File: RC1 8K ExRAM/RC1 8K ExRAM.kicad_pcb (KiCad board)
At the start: 2 copper layers, 99.1 x 83.8 mm, 29 parts, among them J1 Expansion, J2 ADDRESS, U1 74LS138, U2 74LS00, U3 74HC595, U4 74HC595, U5 HM62256BLP-7, U6 74LS244, U7 74LS244, U8 74LS245

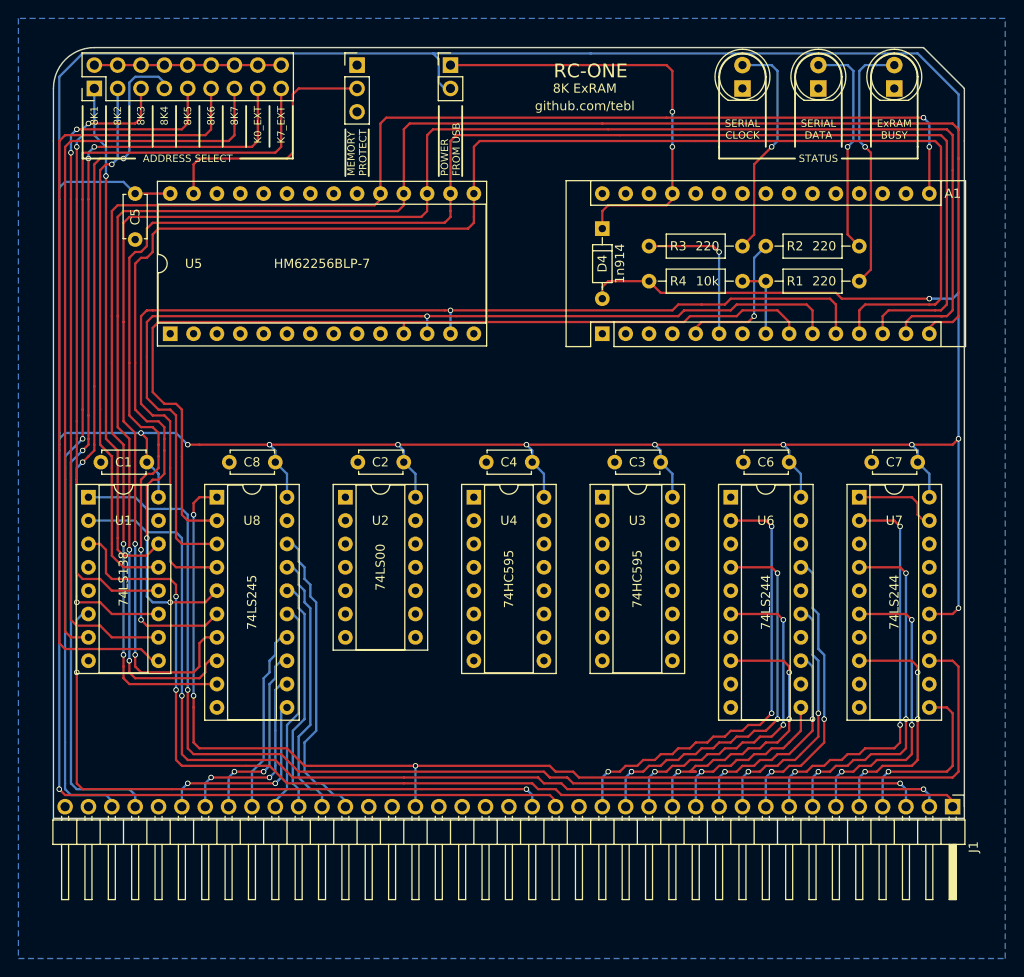
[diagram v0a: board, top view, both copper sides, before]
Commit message: 8K ExRAM layout and silkscreen done
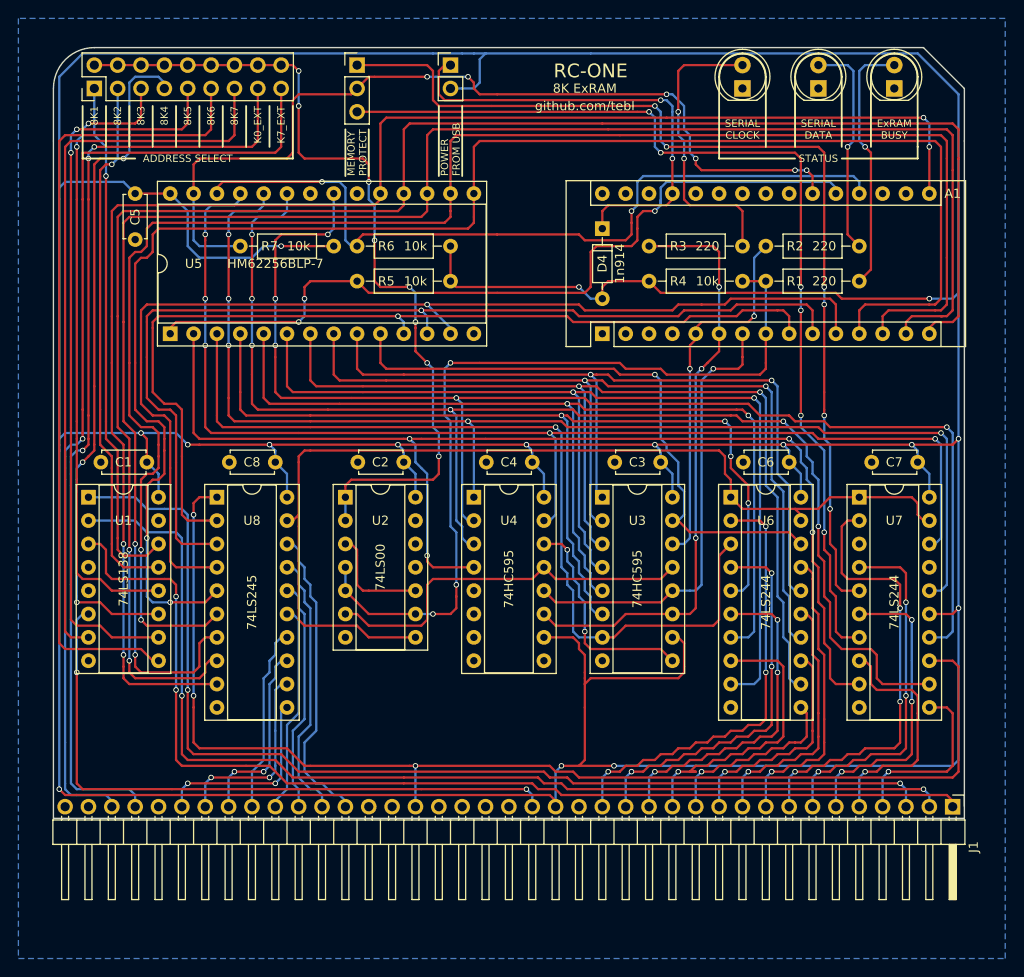
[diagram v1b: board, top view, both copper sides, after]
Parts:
- added R5: 10k, Resistors_THT:R_Axial_DIN0207_L6.3mm_D2.5mm_P10.16mm_Horizontal, F.Cu at (128.3, 90.2)
- added R6: 10k, Resistors_THT:R_Axial_DIN0207_L6.3mm_D2.5mm_P10.16mm_Horizontal, F.Cu at (128.3, 86.4)
- added R7: 10k, Resistors_THT:R_Axial_DIN0207_L6.3mm_D2.5mm_P10.16mm_Horizontal, F.Cu at (115.6, 86.4)
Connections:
- A1 pad 19: (no net) -> /EX_A13
- A1 pad 20: (no net) -> /EX_A14
- A1 pad 21: (no net) -> /EX_R/~W
- U4 pad 7: /EX_R/~W -> (no net)
- U5 pad 1: GND -> /EX_A14
- U5 pad 26: GND -> /EX_A13
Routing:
- net VCC: track 497.4 -> 643.1 mm, vias 12 -> 16
- net /EX_A10: track 0.00 -> 141.6 mm, vias 0 -> 5
- net /EX_A11: track 0.00 -> 140.5 mm, vias 0 -> 6
- net /EX_A9: track 0.00 -> 132.9 mm, vias 0 -> 5
- net /EX_A8: track 0.00 -> 131.6 mm, vias 0 -> 5
- net /EX_A12: track 0.00 -> 126.6 mm, vias 0 -> 4
- net /EX_A4: track 0.00 -> 112.6 mm, vias 0 -> 2
- net /EX_A5: track 0.00 -> 109.9 mm, vias 0 -> 2
- net Net-(JP2-Pad1): track 0.00 -> 108.8 mm, vias 0 -> 6
- net Net-(JP2-Pad3): track 0.00 -> 108.0 mm, vias 0 -> 6
- net /EX_A3: track 0.00 -> 107.0 mm, vias 0 -> 2
- net /EX_A6: track 0.00 -> 106.9 mm, vias 0 -> 4
- net ~EXT_CS: track 9.42 -> 110.4 mm
- net /EX_A2: track 0.00 -> 97.6 mm, vias 0 -> 2
- net /EX_A7: track 0.00 -> 95.3 mm, vias 0 -> 1
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
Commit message: Gerber export
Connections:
- A1 pad 26: (no net) -> /RESET
- J1 pad 20: (no net) -> /RESET
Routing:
- net /RESET: track 0.00 -> 101.1 mm, vias 0 -> 6
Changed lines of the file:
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@@
 (kicad_pcb (version 4) (host pcbnew 4.0.7)
   (general
-    (links 176)
+    (links 177)
     (no_connects 0)
-    (area 91.44 61.595 198.755001 163.830001)
+    (area 95.174999 64.694999 194.385001 148.665001)
     (thickness 1.6)
     (drawings 140)
-    (tracks 1760)
+    (tracks 1793)
     (zones 0)
     (modules 32)
-    (nets 77)
+    (nets 78)
   )
   (page A4)
@@
   (net 75 /EX_A13)
   (net 76 /EX_A14)
+  (net 77 /RESET)
   (net_class Default "This is the default net class."
     (clearance 0.2)
@@
     (add_net /PHI2)
     (add_net /R/~W)
+    (add_net /RESET)
     (add_net BUS_EN)
     (add_net GND)
@@
     (pad 10 thru_hole oval (at 0 22.86 90) (size 1.6 1.6) (drill 0.8) (layers *.Cu *.Mask)
       (net 7 /EX_D1))
-    (pad 26 thru_hole oval (at 15.24 10.16 90) (size 1.6 1.6) (drill 0.8) (layers *.Cu *.Mask))
+    (pad 26 thru_hole oval (at 15.24 10.16 90) (size 1.6 1.6) (drill 0.8) (layers *.Cu *.Mask)
+      (net 77 /RESET))
     (pad 11 thru_hole oval (at 0 25.4 90) (size 1.6 1.6) (drill 0.8) (layers *.Cu *.Mask)
       (net 8 /EX_D2))
@@
     (pad 19 thru_hole oval (at 0 45.72 270) (size 1.7 1.7) (drill 1) (layers *.Cu *.Mask)
       (net 32 /PHI2))
-    (pad 20 thru_hole oval (at 0 48.26 270) (size 1.7 1.7) (drill 1) (layers *.Cu *.Mask))
+    (pad 20 thru_hole oval (at 0 48.26 270) (size 1.7 1.7) (drill 1) (layers *.Cu *.Mask)
+      (net 77 /RESET))
     (pad 21 thru_hole oval (at 0 50.8 270) (size 1.7 1.7) (drill 1) (layers *.Cu *.Mask))
     (pad 22 thru_hole oval (at 0 53.34 270) (size 1.7 1.7) (drill 1) (layers *.Cu *.Mask))
@@
   (segment (start 139.065 123.19) (end 139.065 124.46) (width 0.25) (layer F.Cu) (net 5))
   (segment (start 138.43 116.84) (end 139.065 117.475) (width 0.25) (layer B.Cu) (net 5))
-  (segment (start 136.525 126.365) (end 134.62 126.365) (width 0.25) (layer B.Cu) (net 5))
-  (via (at 136.525 126.365) (size 0.6) (drill 0.4) (layers F.Cu B.Cu) (net 5))
-  (segment (start 138.43 126.365) (end 136.525 126.365) (width 0.25) (layer F.Cu) (net 5))
+  (segment (start 137.16 126.365) (end 134.62 126.365) (width 0.25) (layer B.Cu) (net 5))
+  (via (at 137.16 126.365) (size 0.6) (drill 0.4) (layers F.Cu B.Cu) (net 5))
+  (segment (start 138.43 126.365) (end 137.16 126.365) (width 0.25) (layer F.Cu) (net 5))
   (segment (start 139.065 125.73) (end 138.43 126.365) (width 0.25) (layer F.Cu) (net 5))
   (segment (start 137.795 104.775) (end 137.795 102.87) (width 0.25) (layer B.Cu) (net 5))
@@
   (segment (start 107.95 95.25) (end 108.585 94.615) (width 0.25) (layer F.Cu) (net 76))
   (segment (start 107.95 95.885) (end 107.95 95.25) (width 0.25) (layer F.Cu) (net 76))
+  (segment (start 151.765 90.17) (end 151.765 85.725) (width 0.25) (layer F.Cu) (net 77))
+  (segment (start 152.4 83.185) (end 153.035 83.185) (width 0.25) (layer B.Cu) (net 77))
+  (segment (start 151.765 83.82) (end 152.4 83.185) (width 0.25) (layer B.Cu) (net 77))
+  (segment (start 151.765 85.725) (end 151.765 83.82) (width 0.25) (layer B.Cu) (net 77))
+  (via (at 151.765 85.725) (size 0.6) (drill 0.4) (layers F.Cu B.Cu) (net 77))
+  (segment (start 151.765 95.25) (end 151.765 97.79) (width 0.25) (layer F.Cu) (net 77))
+  (via (at 136.525 123.825) (size 0.6) (drill 0.4) (layers F.Cu B.Cu) (net 77))
+  (segment (start 136.525 123.825) (end 136.525 118.11) (width 0.25) (layer B.Cu) (net 77))
+  (segment (start 136.525 118.11) (end 137.795 116.84) (width 0.25) (layer B.Cu) (net 77))
+  (segment (start 137.795 116.84) (end 137.795 106.045) (width 0.25) (layer B.Cu) (net 77))
+  (segment (start 137.795 106.045) (end 137.16 105.41) (width 0.25) (layer B.Cu) (net 77))
+  (segment (start 137.16 105.41) (end 137.16 99.06) (width 0.25) (layer B.Cu) (net 77))
+  (via (at 137.16 99.06) (size 0.6) (drill 0.4) (layers F.Cu B.Cu) (net 77))
+  (via (at 144.145 142.24) (size 0.6) (drill 0.4) (layers F.Cu B.Cu) (net 77))
+  (segment (start 144.145 142.24) (end 139.065 142.24) (width 0.25) (layer F.Cu) (net 77))
+  (segment (start 144.78 147.32) (end 144.78 142.875) (width 0.25) (layer B.Cu) (net 77))
+  (segment (start 144.78 142.875) (end 144.145 142.24) (width 0.25) (layer B.Cu) (net 77))
+  (segment (start 136.525 127.635) (end 136.525 123.825) (width 0.25) (layer F.Cu) (net 77))
+  (segment (start 136.525 141.605) (end 137.16 142.24) (width 0.25) (layer F.Cu) (net 77))
+  (segment (start 137.16 142.24) (end 139.065 142.24) (width 0.25) (layer F.Cu) (net 77))
+  (segment (start 136.525 127.635) (end 136.525 141.605) (width 0.25) (layer F.Cu) (net 77))
+  (via (at 151.765 90.17) (size 0.6) (drill 0.4) (layers F.Cu B.Cu) (net 77))
+  (segment (start 151.765 90.17) (end 151.765 95.25) (width 0.25) (layer B.Cu) (net 77))
+  (via (at 151.765 95.25) (size 0.6) (drill 0.4) (layers F.Cu B.Cu) (net 77))
+  (segment (start 165.1 81.915) (end 165.1 80.645) (width 0.25) (layer B.Cu) (net 77))
+  (segment (start 153.67 83.185) (end 153.035 83.185) (width 0.25) (layer B.Cu) (net 77))
+  (segment (start 161.29 83.185) (end 153.67 83.185) (width 0.25) (layer B.Cu) (net 77))
+  (segment (start 161.925 82.55) (end 161.29 83.185) (width 0.25) (layer B.Cu) (net 77))
+  (segment (start 164.465 82.55) (end 161.925 82.55) (width 0.25) (layer B.Cu) (net 77))
+  (segment (start 165.1 81.915) (end 164.465 82.55) (width 0.25) (layer B.Cu) (net 77))
+  (segment (start 137.795 98.425) (end 137.16 99.06) (width 0.25) (layer F.Cu) (net 77))
+  (segment (start 151.13 98.425) (end 137.795 98.425) (width 0.25) (layer F.Cu) (net 77))
+  (segment (start 151.765 97.79) (end 151.13 98.425) (width 0.25) (layer F.Cu) (net 77))
   (zone (net 1) (net_name GND) (layer B.Cu) (hatch edge 0.508)
     (connect_pads (clearance 0.508))

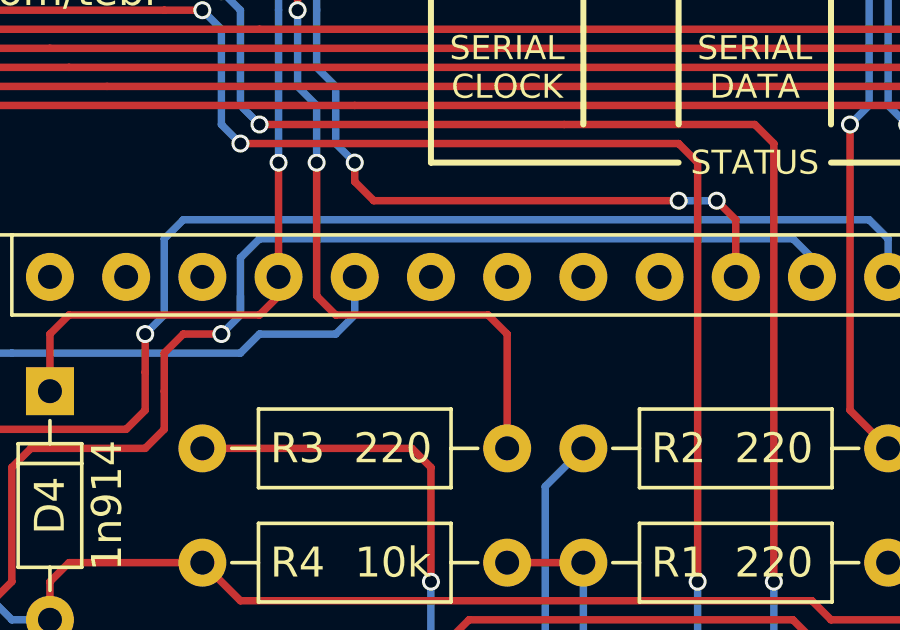
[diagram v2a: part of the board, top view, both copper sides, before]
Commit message: A7 not usable as digital pin on Nano (appearantly)
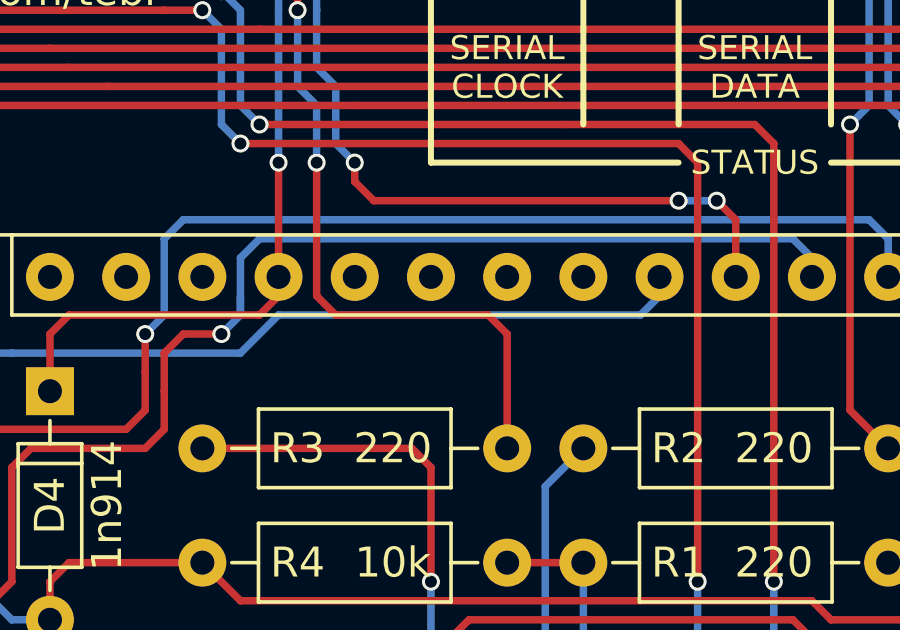
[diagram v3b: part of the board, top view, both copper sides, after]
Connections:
- A1 pad 22: (no net) -> /RESET
- A1 pad 26: /RESET -> (no net)
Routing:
- net /RESET: track 101.1 -> 110.8 mm
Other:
- board text added: "Revision B"
- board text removed: "Revision A"
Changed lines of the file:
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@@
     (pad 6 thru_hole oval (at 0 12.7 90) (size 1.6 1.6) (drill 0.8) (layers *.Cu *.Mask)
       (net 3 SHIFT_CLK))
-    (pad 22 thru_hole oval (at 15.24 20.32 90) (size 1.6 1.6) (drill 0.8) (layers *.Cu *.Mask))
+    (pad 22 thru_hole oval (at 15.24 20.32 90) (size 1.6 1.6) (drill 0.8) (layers *.Cu *.Mask)
+      (net 77 /RESET))
     (pad 7 thru_hole oval (at 0 15.24 90) (size 1.6 1.6) (drill 0.8) (layers *.Cu *.Mask)
       (net 4 SHIFT_LATCH))
@@
     (pad 10 thru_hole oval (at 0 22.86 90) (size 1.6 1.6) (drill 0.8) (layers *.Cu *.Mask)
       (net 7 /EX_D1))
-    (pad 26 thru_hole oval (at 15.24 10.16 90) (size 1.6 1.6) (drill 0.8) (layers *.Cu *.Mask)
-      (net 77 /RESET))
+    (pad 26 thru_hole oval (at 15.24 10.16 90) (size 1.6 1.6) (drill 0.8) (layers *.Cu *.Mask))
     (pad 11 thru_hole oval (at 0 25.4 90) (size 1.6 1.6) (drill 0.8) (layers *.Cu *.Mask)
       (net 8 /EX_D2))
@@
     )
   )
-  (gr_text "Revision A" (at 95.885 145.415) (layer B.SilkS)
+  (gr_text "Revision B" (at 95.885 145.415) (layer B.SilkS)
     (effects (font (size 1 1) (thickness 0.15)) (justify right mirror))
   )
@@
   (segment (start 107.95 95.25) (end 108.585 94.615) (width 0.25) (layer F.Cu) (net 76))
   (segment (start 107.95 95.885) (end 107.95 95.25) (width 0.25) (layer F.Cu) (net 76))
-  (segment (start 151.765 90.17) (end 151.765 85.725) (width 0.25) (layer F.Cu) (net 77))
-  (segment (start 152.4 83.185) (end 153.035 83.185) (width 0.25) (layer B.Cu) (net 77))
-  (segment (start 151.765 83.82) (end 152.4 83.185) (width 0.25) (layer B.Cu) (net 77))
-  (segment (start 151.765 85.725) (end 151.765 83.82) (width 0.25) (layer B.Cu) (net 77))
-  (via (at 151.765 85.725) (size 0.6) (drill 0.4) (layers F.Cu B.Cu) (net 77))
-  (segment (start 151.765 95.25) (end 151.765 97.79) (width 0.25) (layer F.Cu) (net 77))
-  (via (at 136.525 123.825) (size 0.6) (drill 0.4) (layers F.Cu B.Cu) (net 77))
-  (segment (start 136.525 123.825) (end 136.525 118.11) (width 0.25) (layer B.Cu) (net 77))
-  (segment (start 136.525 118.11) (end 137.795 116.84) (width 0.25) (layer B.Cu) (net 77))
-  (segment (start 137.795 116.84) (end 137.795 106.045) (width 0.25) (layer B.Cu) (net 77))
-  (segment (start 137.795 106.045) (end 137.16 105.41) (width 0.25) (layer B.Cu) (net 77))
-  (segment (start 137.16 105.41) (end 137.16 99.06) (width 0.25) (layer B.Cu) (net 77))
-  (via (at 137.16 99.06) (size 0.6) (drill 0.4) (layers F.Cu B.Cu) (net 77))
-  (via (at 144.145 142.24) (size 0.6) (drill 0.4) (layers F.Cu B.Cu) (net 77))
-  (segment (start 144.145 142.24) (end 139.065 142.24) (width 0.25) (layer F.Cu) (net 77))
-  (segment (start 144.78 147.32) (end 144.78 142.875) (width 0.25) (layer B.Cu) (net 77))
-  (segment (start 144.78 142.875) (end 144.145 142.24) (width 0.25) (layer B.Cu) (net 77))
-  (segment (start 136.525 127.635) (end 136.525 123.825) (width 0.25) (layer F.Cu) (net 77))
-  (segment (start 136.525 141.605) (end 137.16 142.24) (width 0.25) (layer F.Cu) (net 77))
-  (segment (start 137.16 142.24) (end 139.065 142.24) (width 0.25) (layer F.Cu) (net 77))
-  (segment (start 136.525 127.635) (end 136.525 141.605) (width 0.25) (layer F.Cu) (net 77))
-  (via (at 151.765 90.17) (size 0.6) (drill 0.4) (layers F.Cu B.Cu) (net 77))
-  (segment (start 151.765 90.17) (end 151.765 95.25) (width 0.25) (layer B.Cu) (net 77))
-  (via (at 151.765 95.25) (size 0.6) (drill 0.4) (layers F.Cu B.Cu) (net 77))
-  (segment (start 165.1 81.915) (end 165.1 80.645) (width 0.25) (layer B.Cu) (net 77))
-  (segment (start 153.67 83.185) (end 153.035 83.185) (width 0.25) (layer B.Cu) (net 77))
-  (segment (start 161.29 83.185) (end 153.67 83.185) (width 0.25) (layer B.Cu) (net 77))
-  (segment (start 161.925 82.55) (end 161.29 83.185) (width 0.25) (layer B.Cu) (net 77))
-  (segment (start 164.465 82.55) (end 161.925 82.55) (width 0.25) (layer B.Cu) (net 77))
-  (segment (start 165.1 81.915) (end 164.465 82.55) (width 0.25) (layer B.Cu) (net 77))
-  (segment (start 137.795 98.425) (end 137.16 99.06) (width 0.25) (layer F.Cu) (net 77))
-  (segment (start 151.13 98.425) (end 137.795 98.425) (width 0.25) (layer F.Cu) (net 77))
+  (segment (start 161.29 83.185) (end 162.56 81.915) (width 0.25) (layer B.Cu) (net 77))
   (segment (start 151.765 97.79) (end 151.13 98.425) (width 0.25) (layer F.Cu) (net 77))
+  (segment (start 151.13 98.425) (end 137.795 98.425) (width 0.25) (layer F.Cu) (net 77))
+  (segment (start 137.795 98.425) (end 137.16 99.06) (width 0.25) (layer F.Cu) (net 77))
+  (segment (start 161.29 83.185) (end 153.67 83.185) (width 0.25) (layer B.Cu) (net 77))
+  (segment (start 153.67 83.185) (end 153.035 83.185) (width 0.25) (layer B.Cu) (net 77))
+  (via (at 151.765 95.25) (size 0.6) (drill 0.4) (layers F.Cu B.Cu) (net 77))
+  (segment (start 151.765 90.17) (end 151.765 95.25) (width 0.25) (layer B.Cu) (net 77))
+  (via (at 151.765 90.17) (size 0.6) (drill 0.4) (layers F.Cu B.Cu) (net 77))
+  (segment (start 136.525 127.635) (end 136.525 141.605) (width 0.25) (layer F.Cu) (net 77))
+  (segment (start 137.16 142.24) (end 139.065 142.24) (width 0.25) (layer F.Cu) (net 77))
+  (segment (start 136.525 141.605) (end 137.16 142.24) (width 0.25) (layer F.Cu) (net 77))
+  (segment (start 136.525 127.635) (end 136.525 123.825) (width 0.25) (layer F.Cu) (net 77))
+  (segment (start 144.78 142.875) (end 144.145 142.24) (width 0.25) (layer B.Cu) (net 77))
+  (segment (start 144.78 147.32) (end 144.78 142.875) (width 0.25) (layer B.Cu) (net 77))
+  (segment (start 144.145 142.24) (end 139.065 142.24) (width 0.25) (layer F.Cu) (net 77))
+  (via (at 144.145 142.24) (size 0.6) (drill 0.4) (layers F.Cu B.Cu) (net 77))
+  (via (at 137.16 99.06) (size 0.6) (drill 0.4) (layers F.Cu B.Cu) (net 77))
+  (segment (start 137.16 105.41) (end 137.16 99.06) (width 0.25) (layer B.Cu) (net 77))
+  (segment (start 137.795 106.045) (end 137.16 105.41) (width 0.25) (layer B.Cu) (net 77))
+  (segment (start 137.795 116.84) (end 137.795 106.045) (width 0.25) (layer B.Cu) (net 77))
+  (segment (start 136.525 118.11) (end 137.795 116.84) (width 0.25) (layer B.Cu) (net 77))
+  (segment (start 136.525 123.825) (end 136.525 118.11) (width 0.25) (layer B.Cu) (net 77))
+  (via (at 136.525 123.825) (size 0.6) (drill 0.4) (layers F.Cu B.Cu) (net 77))
+  (segment (start 151.765 95.25) (end 151.765 97.79) (width 0.25) (layer F.Cu) (net 77))
+  (via (at 151.765 85.725) (size 0.6) (drill 0.4) (layers F.Cu B.Cu) (net 77))
+  (segment (start 151.765 85.725) (end 151.765 83.82) (width 0.25) (layer B.Cu) (net 77))
+  (segment (start 151.765 83.82) (end 152.4 83.185) (width 0.25) (layer B.Cu) (net 77))
+  (segment (start 152.4 83.185) (end 153.035 83.185) (width 0.25) (layer B.Cu) (net 77))
+  (segment (start 151.765 90.17) (end 151.765 85.725) (width 0.25) (layer F.Cu) (net 77))
+  (segment (start 174.625 81.915) (end 175.26 81.28) (width 0.25) (layer B.Cu) (net 77))
+  (segment (start 162.56 81.915) (end 174.625 81.915) (width 0.25) (layer B.Cu) (net 77))
+  (segment (start 175.26 81.28) (end 175.26 80.645) (width 0.25) (layer B.Cu) (net 77))
   (zone (net 1) (net_name GND) (layer B.Cu) (hatch edge 0.508)
     (connect_pads (clearance 0.508))
